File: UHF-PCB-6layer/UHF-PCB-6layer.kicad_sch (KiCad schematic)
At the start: 5 parts, among them U1 XC7A100T-CSG324, U2 MC100EPT22D, U3 TAV1-331+, U4 TPS3103K33DBVR, U5 XMSM0G3507SPT

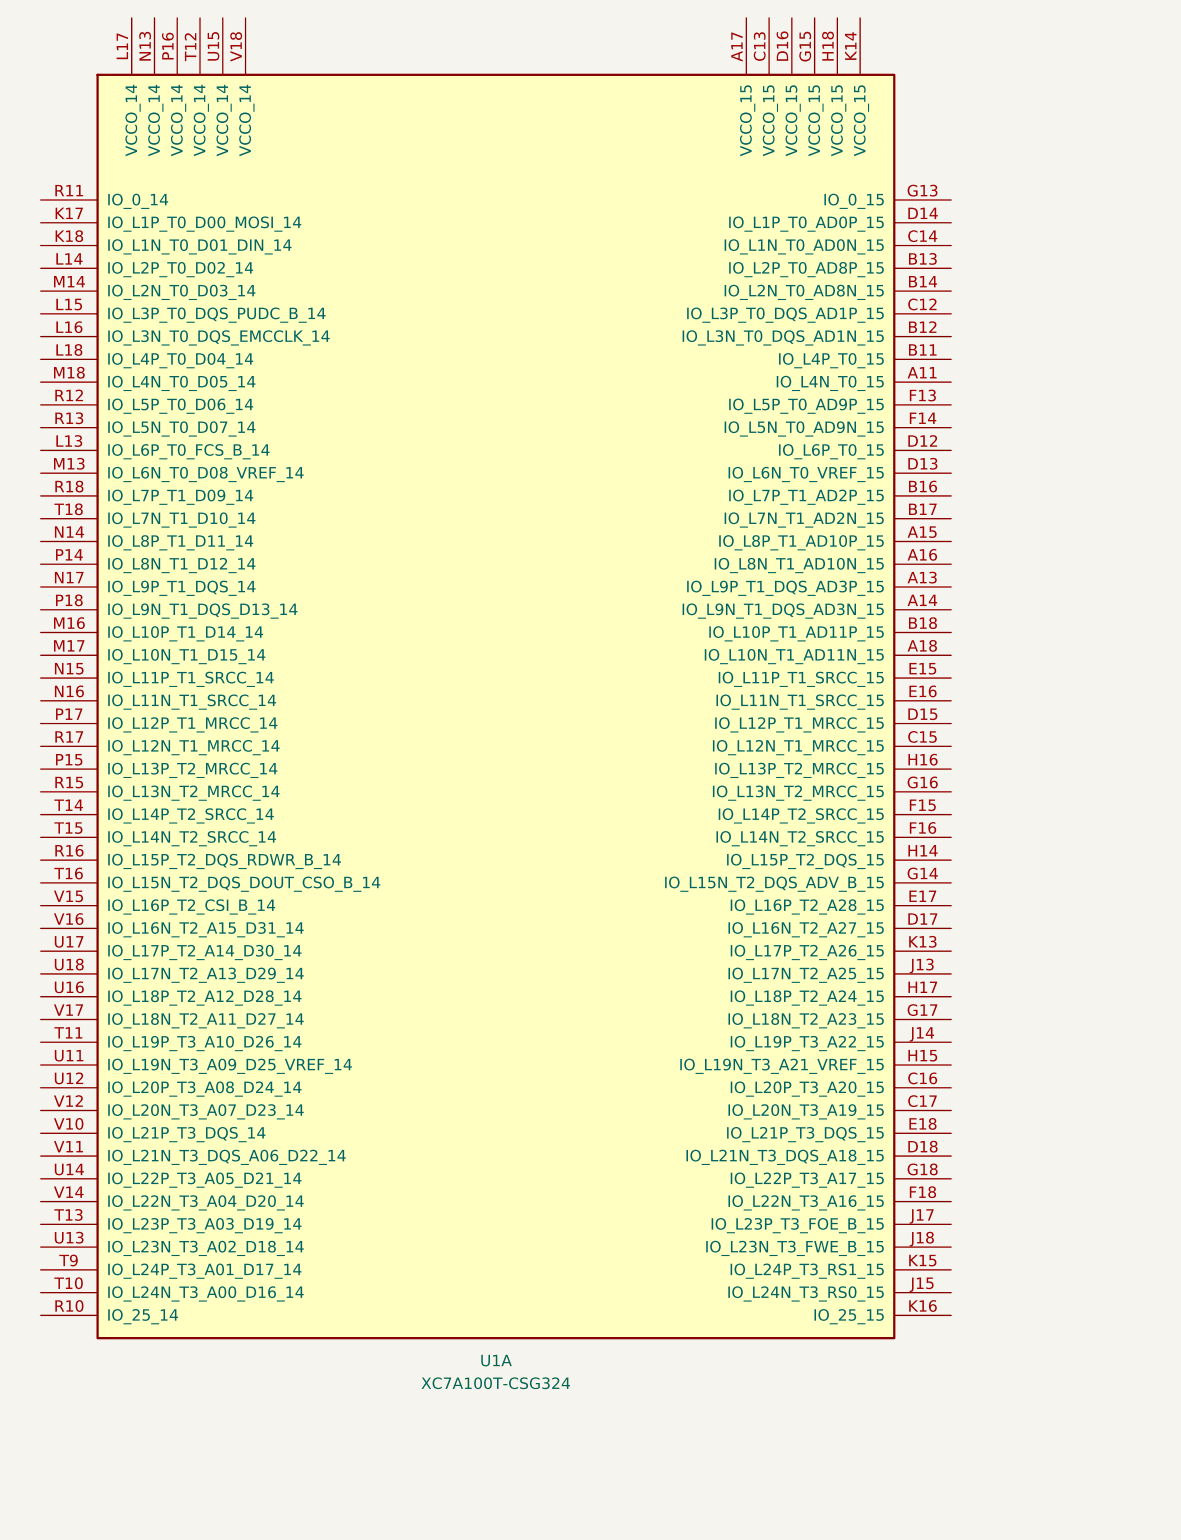
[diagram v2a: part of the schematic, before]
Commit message: added XA7A to schematic
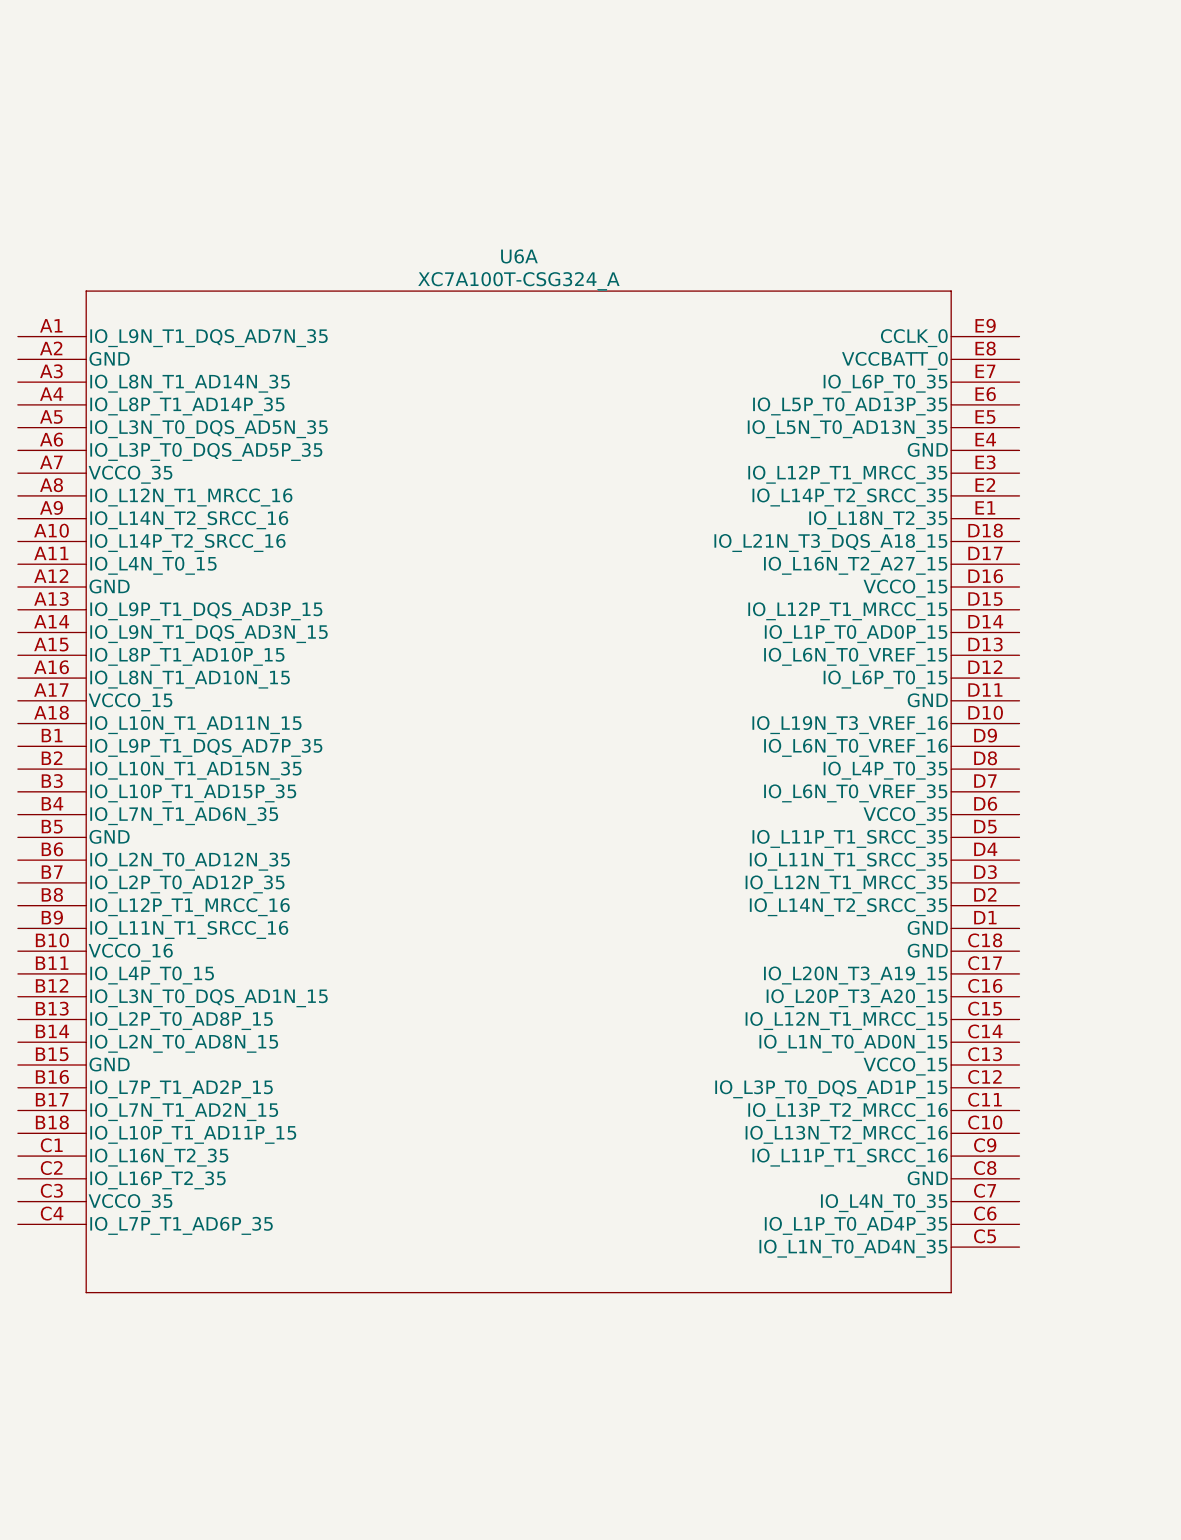
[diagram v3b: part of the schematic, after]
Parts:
- removed U1: XC7A100T-CSG324, symbol FPGA_Xilinx_Artix7:XC7A100T-CSG324
- added U6: XC7A100T-CSG324_A, CS/CSG324_XIL, symbol 2023-12-18_23-40-33:XC7A100T-CSG324_A

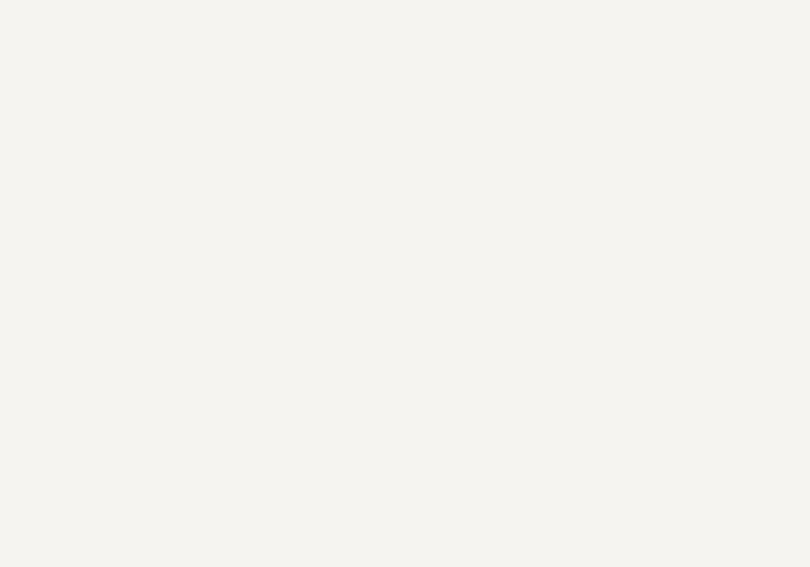
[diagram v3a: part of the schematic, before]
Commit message: added mixer
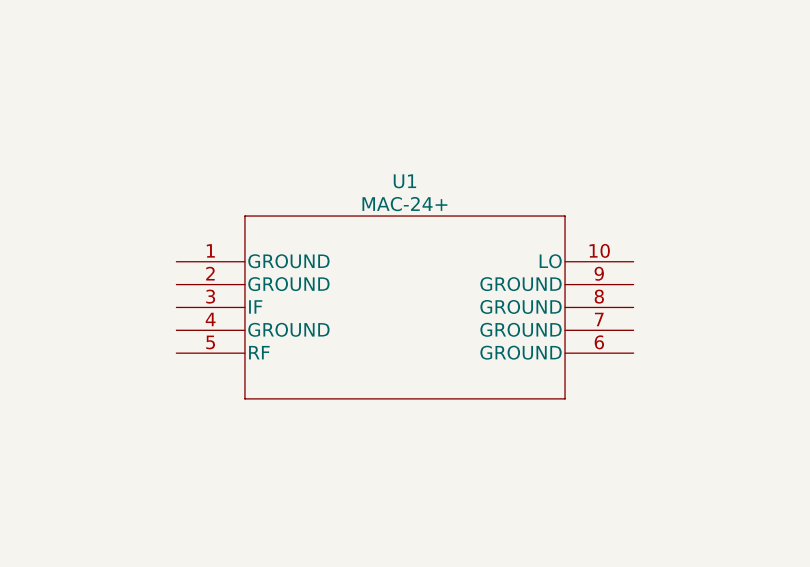
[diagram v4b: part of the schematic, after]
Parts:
- added U1: MAC-24+, DZ1650_MNC, symbol 2023-12-20_00-32-43:MAC-24+
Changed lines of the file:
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@@
     (rev "MK1")
+  )
+  (symbol (lib_id "2023-12-20_00-32-43:MAC-24+") (at 298.45 83.82 0) (unit 1)
+    (in_bom yes) (on_board yes) (dnp no) (fields_autoplaced)
+    (property "Reference" "U1" (at 323.85 74.93 0)
+      (effects (font (size 1.524 1.524)))
+    )
+    (property "Value" "MAC-24+" (at 323.85 77.47 0)
+      (effects (font (size 1.524 1.524)))
+    )
+    (property "Footprint" "DZ1650_MNC" (at 323.85 77.724 0)
+      (effects (font (size 1.524 1.524)) hide)
+    )
+    (property "Datasheet" "" (at 298.45 83.82 0)
+      (effects (font (size 1.524 1.524)))
+    )
+    (pin "1")
+    (pin "10")
+    (pin "2")
+    (pin "3")
+    (pin "4")
+    (pin "5")
+    (pin "6")
+    (pin "7")
+    (pin "8")
+    (pin "9")
+    (instances
+      (project "UHF-PCB-6layer"
+        (path "/408f5dbf-8c57-4b84-b0cc-1d788fcf6d08"
+          (reference "U1") (unit 1)
+        )
+      )
+    )
   )
   (symbol (lib_id "2023-12-16_21-42-08:TAV1-331+") (at 378.46 52.07 0) (unit 1)

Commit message: added required caps and resistors for microcontroller
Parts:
- added C1: 0.1uf, Capacitor_SMD:C_0603_1608Metric, symbol Device:C
- added C2, C5: 10uf, Capacitor_SMD:C_0603_1608Metric, symbol Device:C
- added C3: C, Capacitor_SMD:C_0603_1608Metric, symbol Device:C
- added R1: 47k, symbol Device:R
- added R2: 100k, symbol Device:R
- added R3, R4: 4.7k, symbol Device:R
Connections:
- net at U5.1 (PA0_/_FCC_IN): now also R3.2
- net at U5.2 (PA1): now also R4.2
- net at U5.4 (NRST): now also C5.2, R1.1
- net at U5.48 (VCORE): now also C3.1
- net +3.3V: now reaches U5.6 (VDD)
- net +3.3V: now also C1.2, C2.2, R1.2
- net GNDREF: now reaches U5.7 (VSS)
- net GNDREF: now also C1.1, C2.1, C3.2, C5.1, R2.1
- net at U5.8 (PA2_/_ROSC): now also R2.2
- new net +5V: R3.1, R4.1
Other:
- moved on the sheet: U1, U2, U3, U4, U5

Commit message: added footprints for resistors
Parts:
- R1, R2, R3, R4: footprint (none) -> Resistor_SMD:R_0603_1608Metric
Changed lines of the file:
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@@
       (effects (font (size 1.27 1.27)) (justify left))
     )
-    (property "Footprint" "" (at 85.852 176.53 90)
+    (property "Footprint" "Resistor_SMD:R_0603_1608Metric" (at 85.852 176.53 90)
       (effects (font (size 1.27 1.27)) hide)
     )
@@
       (effects (font (size 1.27 1.27)) (justify left))
     )
-    (property "Footprint" "" (at 121.412 163.83 90)
+    (property "Footprint" "Resistor_SMD:R_0603_1608Metric" (at 121.412 163.83 90)
       (effects (font (size 1.27 1.27)) hide)
     )
@@
       (effects (font (size 1.27 1.27)))
     )
-    (property "Footprint" "" (at 105.41 194.818 90)
+    (property "Footprint" "Resistor_SMD:R_0603_1608Metric" (at 105.41 194.818 90)
       (effects (font (size 1.27 1.27)) hide)
     )
@@
       (effects (font (size 1.27 1.27)) (justify left))
     )
-    (property "Footprint" "" (at 125.222 163.83 90)
-      (effects (font (size 1.27 1.27)) hide)
-    )
+    (property "Footprint" "Resistor_SMD:R_0603_1608Metric" (at 125.222 163.83 90)
+      (effects (font (size 1.27 1.27)) hide)
+    )

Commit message: moved stuff around
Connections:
- net GNDREF: now also U3.1 (GND), U3.3 (GND)
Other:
- moved on the sheet: U4
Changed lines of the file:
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@@
+    (stroke (width 0) (type default))
+  )
+  (wire (pts (xy 259.08 90.17) (xy 259.08 93.98))
     (stroke (width 0) (type default))
   )
@@
   )
   (wire (pts (xy 247.65 161.29) (xy 247.65 162.56))
+    (stroke (width 0) (type default))
+  )
+  (wire (pts (xy 304.8 96.52) (xy 304.8 100.33))
     (stroke (width 0) (type default))
   )
@@
         (path "/408f5dbf-8c57-4b84-b0cc-1d788fcf6d08"
           (reference "C1") (unit 1)
+        )
+      )
+    )
+  )
+  (symbol (lib_id "power:GNDREF") (at 259.08 90.17 180) (unit 1)
+    (in_bom yes) (on_board yes) (dnp no) (fields_autoplaced)
+    (property "Reference" "#PWR07" (at 259.08 83.82 0)
+      (effects (font (size 1.27 1.27)) hide)
+    )
+    (property "Value" "GNDREF" (at 259.08 86.36 0)
+      (effects (font (size 1.27 1.27)))
+    )
+    (property "Footprint" "" (at 259.08 90.17 0)
+      (effects (font (size 1.27 1.27)) hide)
+    )
+    (property "Datasheet" "" (at 259.08 90.17 0)
+      (effects (font (size 1.27 1.27)) hide)
+    )
+    (pin "1")
+    (instances
+      (project "UHF-PCB-6layer"
+        (path "/408f5dbf-8c57-4b84-b0cc-1d788fcf6d08"
+          (reference "#PWR07") (unit 1)
+        )
+      )
+    )
+  )
+  (symbol (lib_id "power:GNDREF") (at 304.8 100.33 0) (unit 1)
+    (in_bom yes) (on_board yes) (dnp no) (fields_autoplaced)
+    (property "Reference" "#PWR06" (at 304.8 106.68 0)
+      (effects (font (size 1.27 1.27)) hide)
+    )
+    (property "Value" "GNDREF" (at 304.8 105.41 0)
+      (effects (font (size 1.27 1.27)))
+    )
+    (property "Footprint" "" (at 304.8 100.33 0)
+      (effects (font (size 1.27 1.27)) hide)
+    )
+    (property "Datasheet" "" (at 304.8 100.33 0)
+      (effects (font (size 1.27 1.27)) hide)
+    )
+    (pin "1")
+    (instances
+      (project "UHF-PCB-6layer"
+        (path "/408f5dbf-8c57-4b84-b0cc-1d788fcf6d08"
+          (reference "#PWR06") (unit 1)
         )
       )
@@
     )
   )
-  (symbol (lib_id "TPS3103K33DBVR:TPS3103K33DBVR") (at 274.32 201.93 0) (unit 1)
-    (in_bom yes) (on_board yes) (dnp no) (fields_autoplaced)
-    (property "Reference" "U4" (at 274.32 187.96 0)
-      (effects (font (size 1.27 1.27)))
-    )
-    (property "Value" "TPS3103K33DBVR" (at 274.32 190.5 0)
-      (effects (font (size 1.27 1.27)))
-    )
-    (property "Footprint" "SOT95P280X145-6N" (at 274.32 201.93 0)
+  (symbol (lib_id "TPS3103K33DBVR:TPS3103K33DBVR") (at 57.15 167.64 0) (mirror x) (unit 1)
+    (in_bom yes) (on_board yes) (dnp no)
+    (property "Reference" "U4" (at 57.15 181.61 0)
+      (effects (font (size 1.27 1.27)))
+    )
+    (property "Value" "TPS3103K33DBVR" (at 57.15 179.07 0)
+      (effects (font (size 1.27 1.27)))
+    )
+    (property "Footprint" "SOT95P280X145-6N" (at 57.15 167.64 0)
       (effects (font (size 1.27 1.27)) (justify left bottom) hide)
     )
-    (property "Datasheet" "" (at 274.32 201.93 0)
+    (property "Datasheet" "" (at 57.15 167.64 0)
       (effects (font (size 1.27 1.27)) (justify left bottom) hide)
     )
